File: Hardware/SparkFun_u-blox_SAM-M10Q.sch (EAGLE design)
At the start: 34 parts, among them J1 Qwiic Right Angle, J2 Qwiic Right Angle, J4 BOOT, U1 U-BLOX_SAM_M10Q-00B

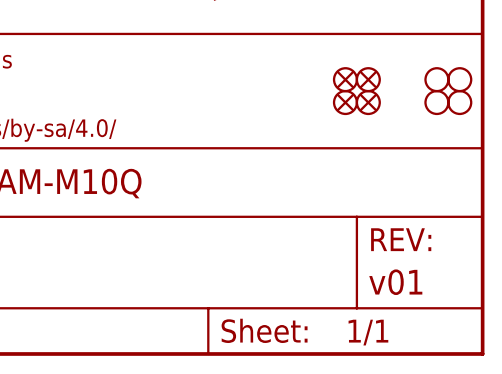
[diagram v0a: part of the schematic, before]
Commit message: Update for v10, Panelize. Add measures.
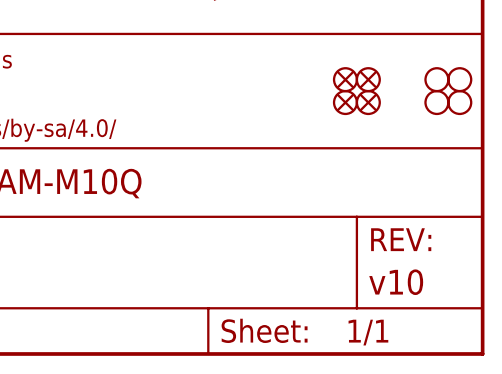
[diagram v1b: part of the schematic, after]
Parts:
- FRAME1: REV v01 -> v10
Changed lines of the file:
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@@
 <part name="FRAME1" library="SparkFun-Aesthetics" deviceset="FRAME-LETTER" device="">
 <attribute name="DESIGNER" value="Alex Brudner"/>
-<attribute name="REV" value="v01"/>
+<attribute name="REV" value="v10"/>
 </part>
 <part name="FD1" library="SparkFun-Aesthetics" deviceset="FIDUCIAL" device="UFIDUCIAL"/>

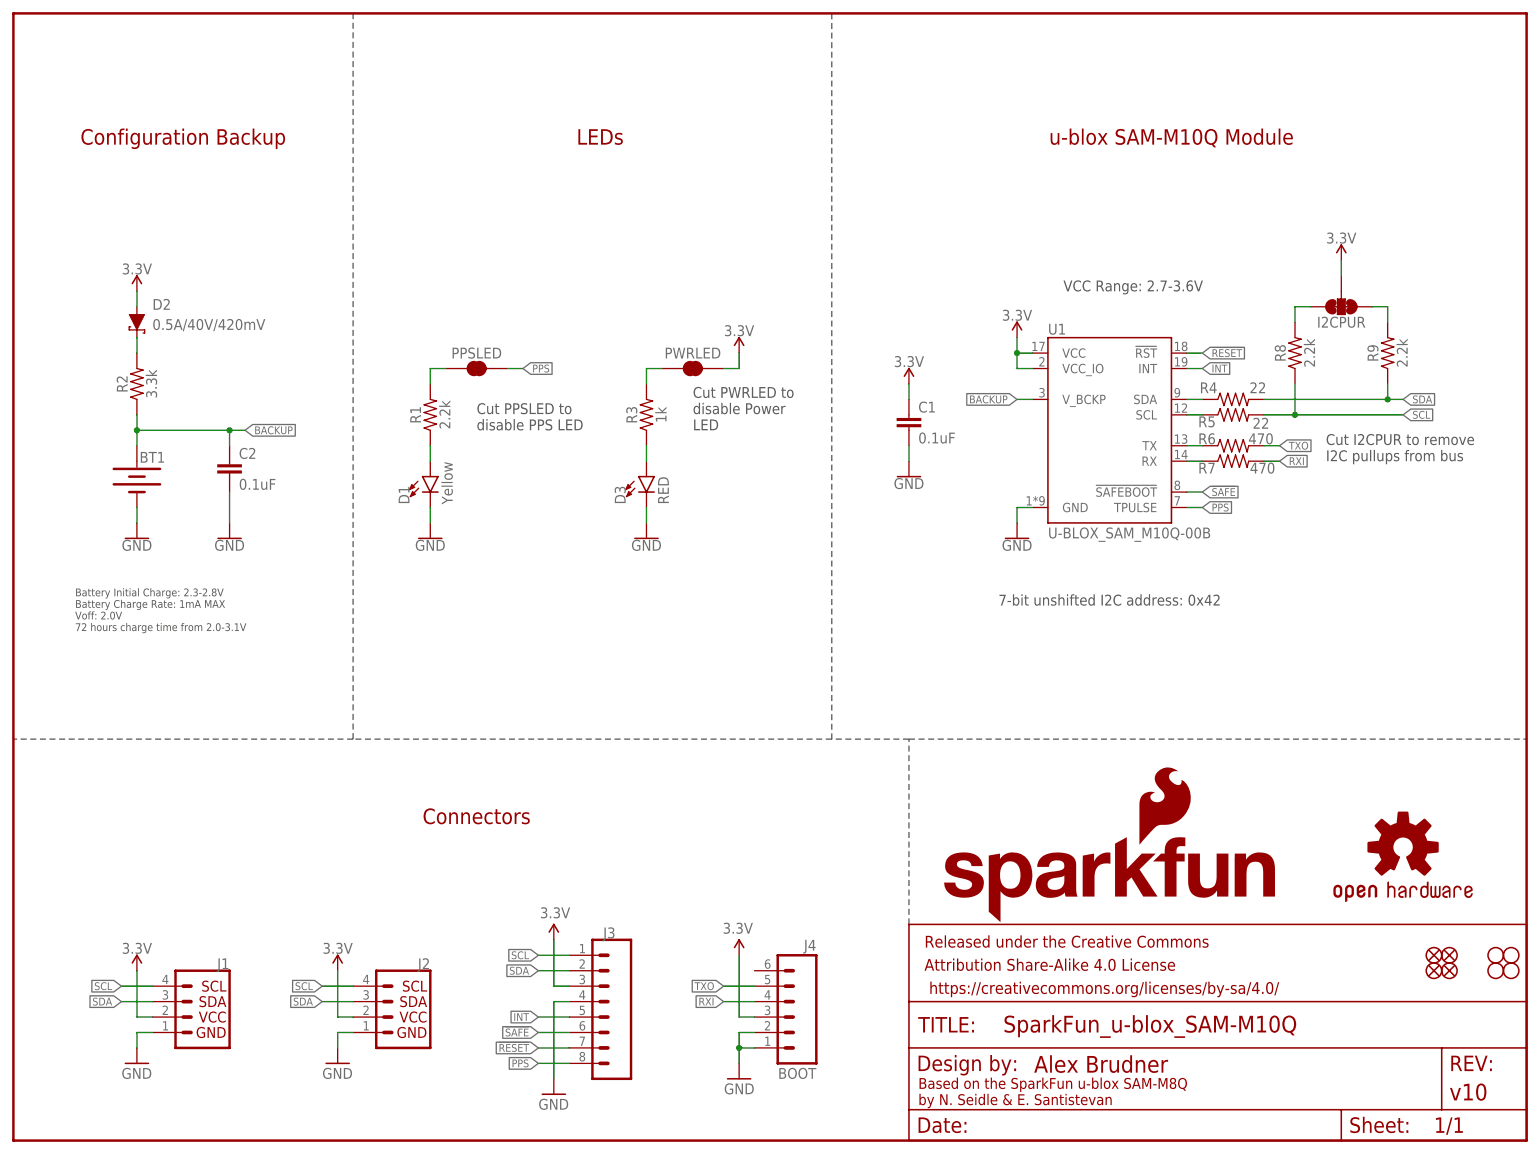
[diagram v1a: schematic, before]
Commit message: Update post design review.
Swap for updated reflowable battery.
Adjust note for battery accordingly.
Add qwiic symbol in schematic, replacing silk only on board.
Expand t/b keepout under M10Q.
Swap SCL/SDA silk so they are on the correct pins.
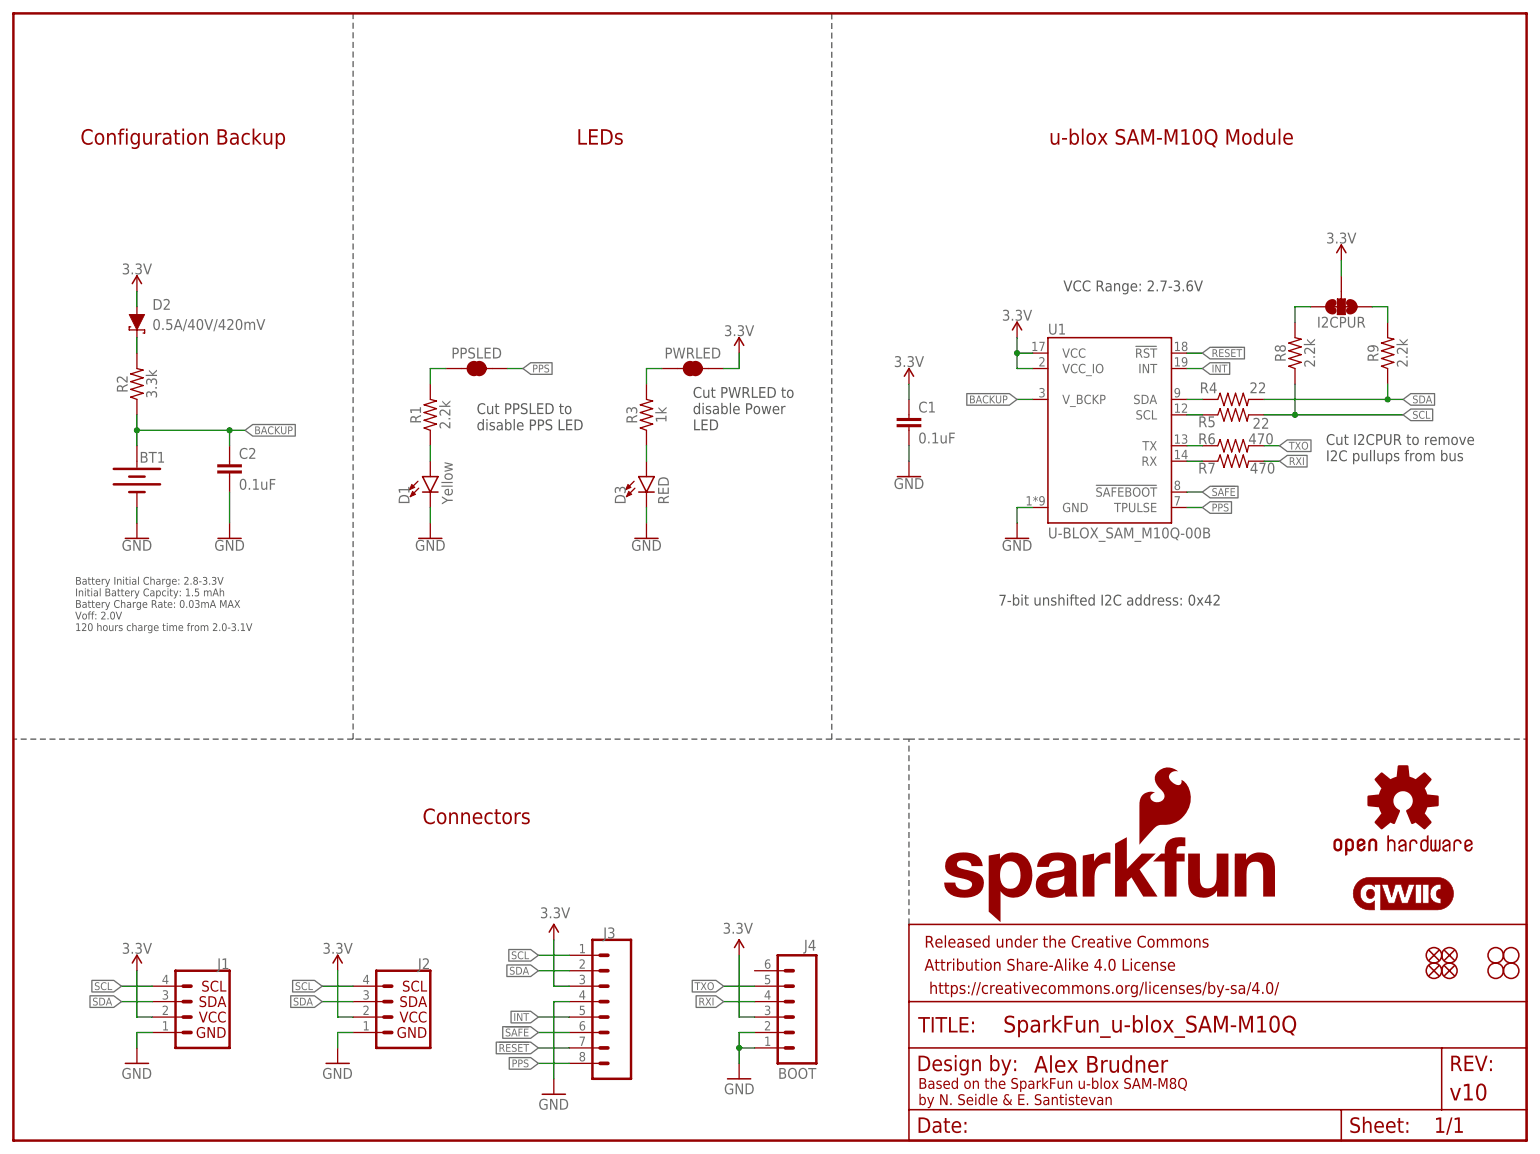
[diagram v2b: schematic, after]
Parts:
- added LOGO3: QWIIC_LOGO_CONNECTOR, SparkFun-Aesthetics:QWIIC_LOGO_CONNECTOR
- BT1: device SparkFun-Batteries:ML414H_IV01E_BATTERY -> SparkFun-Batteries:RELOWABLE_BATTERY_MS421R
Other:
- note added: "Battery Initial Charge: 2.8-3.3V Initial Battery Capcity: 1.5 mAh Battery Charge Rate: 0.03mA MAX Voff: 2.0V 120 hours charge time from 2.0-3.1V"
- note removed: "Battery Initial Charge: 2.3-2.8V Battery Charge Rate: 1mA MAX Voff: 2.0V 72 hours charge time from 2.0-3.1V"
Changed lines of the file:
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@@
 <part name="LOGO1" library="SparkFun-Aesthetics" deviceset="OSHW-LOGO" device="M"/>
 <part name="LOGO2" library="SparkFun-Aesthetics" deviceset="SFE_LOGO_NAME_FLAME" device=".2_INCH"/>
-<part name="BT1" library="SparkFun-Batteries" deviceset="ML414H_IV01E_BATTERY" device="" value="6.8MM_COIN_CELL"/>
+<part name="BT1" library="SparkFun-Batteries" deviceset="RELOWABLE_BATTERY" device="_MS421R" value="6.8MM_COIN_CELL"/>
 <part name="GND2" library="SparkFun-PowerSymbols" deviceset="GND" device=""/>
 <part name="GND4" library="SparkFun-PowerSymbols" deviceset="GND" device=""/>
@@
 <part name="C1" library="SparkFun-Capacitors" deviceset="0.1UF" device="-0603-25V-(+80/-20%)" value="0.1uF"/>
 <part name="C2" library="SparkFun-Capacitors" deviceset="0.1UF" device="-0603-25V-(+80/-20%)" value="0.1uF"/>
+<part name="LOGO3" library="SparkFun-Aesthetics" deviceset="QWIIC_LOGO" device="_CONNECTOR"/>
 </parts>
 <sheets>
@@
 <text x="148.844" y="5.842" size="1.778" layer="94" font="vector">Based on the SparkFun u-blox SAM-M8Q
 by N. Seidle &amp; E. Santistevan</text>
-<text x="10.16" y="83.82" size="1.27" layer="97" font="vector">Battery Initial Charge: 2.3-2.8V
-Battery Charge Rate: 1mA MAX
+<text x="10.16" y="83.82" size="1.27" layer="97" font="vector">Battery Initial Charge: 2.8-3.3V
+Initial Battery Capcity: 1.5 mAh
+Battery Charge Rate: 0.03mA MAX
 Voff: 2.0V
-72 hours charge time from 2.0-3.1V</text>
+120 hours charge time from 2.0-3.1V</text>
 <text x="180.34" y="88.9" size="1.778" layer="97" font="vector" align="center">7-bit unshifted I2C address: 0x42</text>
 <text x="215.9" y="111.76" size="1.778" layer="97" font="vector">Cut I2CPUR to remove
@@
 <instance part="H3" gate="G$1" x="243.84" y="27.94" smashed="yes"/>
 <instance part="H4" gate="G$1" x="243.84" y="30.48" smashed="yes"/>
-<instance part="LOGO1" gate="G$1" x="228.6" y="48.26" smashed="yes"/>
+<instance part="LOGO1" gate="G$1" x="228.6" y="55.88" smashed="yes"/>
 <instance part="LOGO2" gate="G$1" x="152.4" y="35.56" smashed="yes"/>
 <instance part="BT1" gate="G$1" x="20.32" y="109.22" smashed="yes" rot="R270">
@@
 <attribute name="VALUE" x="37.084" y="107.061" size="1.778" layer="96" font="vector"/>
 </instance>
+<instance part="LOGO3" gate="G$1" x="228.6" y="40.64" smashed="yes"/>
 </instances>
 <busses>

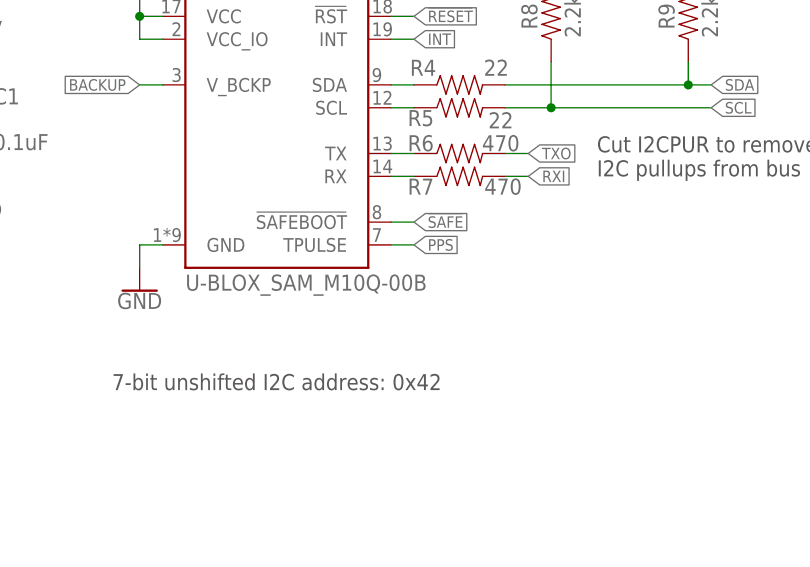
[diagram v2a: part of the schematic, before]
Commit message: Rework paste for DFM experiment.
Move original panel into 100_paste folder.
Repanelize with quad box paste and put into quad_paste folder.
Update library to have new variant.
Update sch and brd with new part.
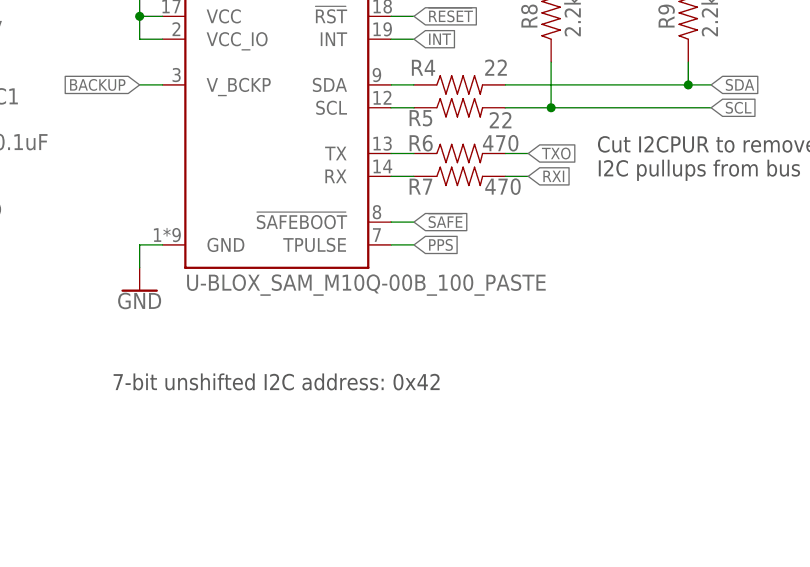
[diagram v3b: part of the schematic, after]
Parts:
- U1: value U-BLOX_SAM_M10Q-00B -> U-BLOX_SAM_M10Q-00B_100_PASTE; device u-blox_SAM-M10Q:U-BLOX_SAM_M10Q-00B -> u-blox_SAM-M10Q:U-BLOX_SAM_M10Q-00B_100_PASTE
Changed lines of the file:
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@@
 <part name="R5" library="SparkFun-Resistors" deviceset="22OHM" device="-0603-1/10W-1%" value="22"/>
 <part name="SUPPLY7" library="SparkFun-PowerSymbols" deviceset="3.3V" device=""/>
-<part name="U1" library="u-blox_SAM-M10Q" deviceset="U-BLOX_SAM_M10Q-00B" device=""/>
+<part name="U1" library="u-blox_SAM-M10Q" deviceset="U-BLOX_SAM_M10Q-00B" device="_100_PASTE" value="U-BLOX_SAM_M10Q-00B_100_PASTE"/>
 <part name="GND1" library="SparkFun-PowerSymbols" deviceset="GND" device=""/>
 <part name="D1" library="SparkFun-LED" deviceset="LED-YELLOW" device="0603" value="Yellow"/>

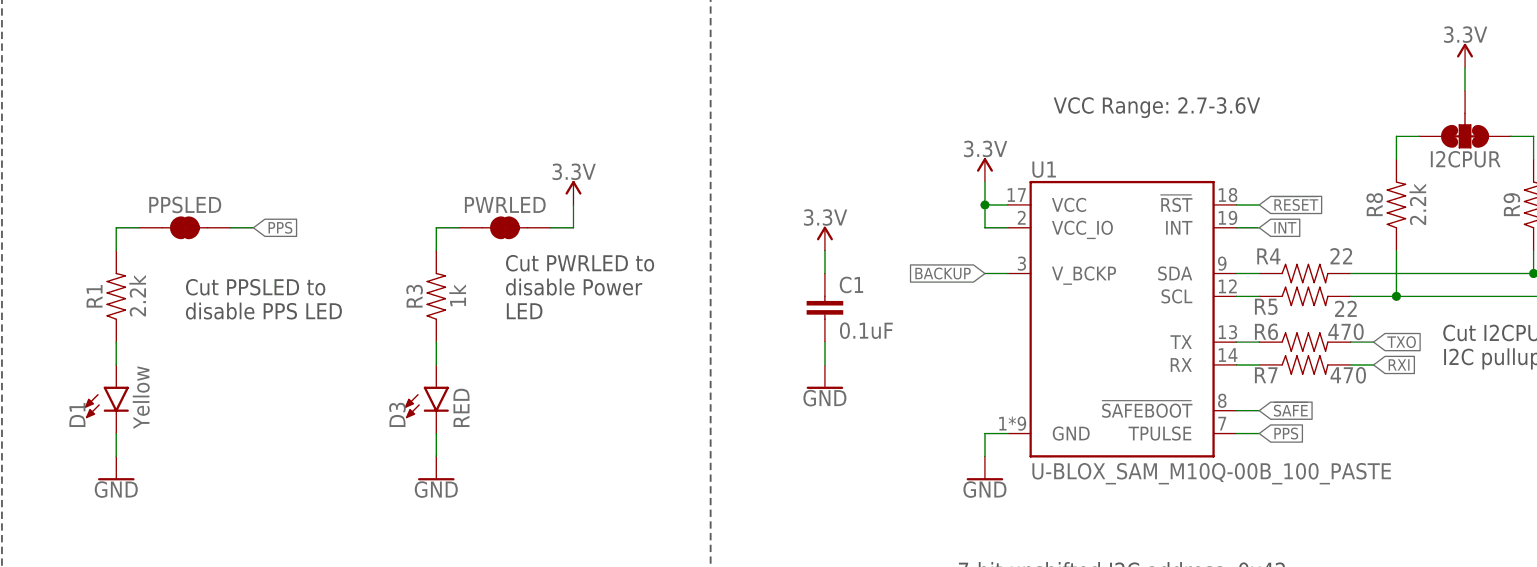
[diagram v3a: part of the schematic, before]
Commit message: Update for release
Remove quad paste part from lib.
Remove quad paste production folder.
Move 100 paste up one folder.
Update schematic/board for new part.
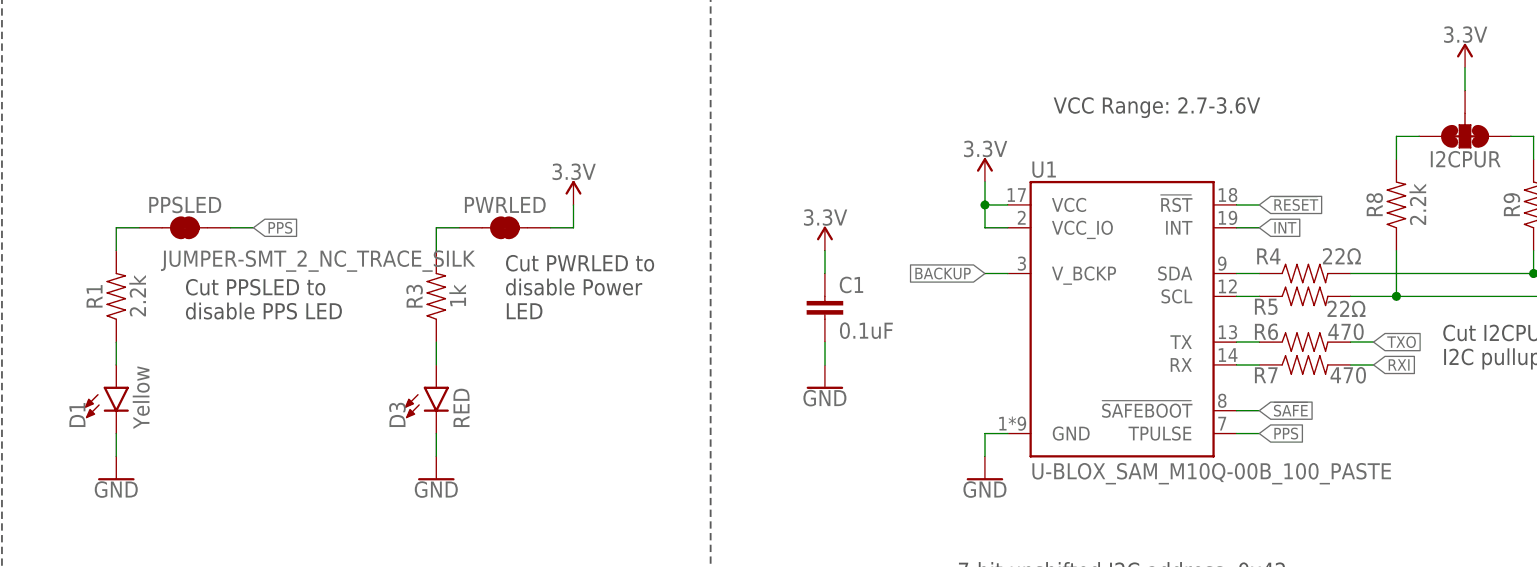
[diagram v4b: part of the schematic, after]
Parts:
- R4, R5: value 22 -> 22Ω
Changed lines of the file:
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@@
 <part name="R8" library="SparkFun-Resistors" deviceset="2.2KOHM" device="-0603-1/10W-1%" value="2.2k"/>
 <part name="R9" library="SparkFun-Resistors" deviceset="2.2KOHM" device="-0603-1/10W-1%" value="2.2k"/>
-<part name="I2CPUR" library="SparkFun-Jumpers" deviceset="JUMPER-SMT_3_2-NC_TRACE" device="_SILK" value="JUMPER-SMT_3_2-NC_TRACE_SILK"/>
+<part name="I2CPUR" library="SparkFun-Jumpers" deviceset="JUMPER-SMT_3_2-NC_TRACE" device="_SILK" package3d_urn="urn:adsk.eagle:package:39289/1" value="JUMPER-SMT_3_2-NC_TRACE_SILK"/>
 <part name="SUPPLY9" library="SparkFun-PowerSymbols" deviceset="3.3V" device=""/>
-<part name="R4" library="SparkFun-Resistors" deviceset="22OHM" device="-0603-1/10W-1%" value="22"/>
-<part name="R5" library="SparkFun-Resistors" deviceset="22OHM" device="-0603-1/10W-1%" value="22"/>
+<part name="R4" library="SparkFun-Resistors" deviceset="22OHM" device="-0603-1/10W-1%" value="22Ω"/>
+<part name="R5" library="SparkFun-Resistors" deviceset="22OHM" device="-0603-1/10W-1%" value="22Ω"/>
 <part name="SUPPLY7" library="SparkFun-PowerSymbols" deviceset="3.3V" device=""/>
 <part name="U1" library="u-blox_SAM-M10Q" deviceset="U-BLOX_SAM_M10Q-00B" device="_100_PASTE" value="U-BLOX_SAM_M10Q-00B_100_PASTE"/>
 <part name="GND1" library="SparkFun-PowerSymbols" deviceset="GND" device=""/>
 <part name="D1" library="SparkFun-LED" deviceset="LED-YELLOW" device="0603" value="Yellow"/>
-<part name="PPSLED" library="SparkFun-Jumpers" deviceset="JUMPER-SMT_2_NC_TRACE" device="_SILK" value=""/>
+<part name="PPSLED" library="SparkFun-Jumpers" deviceset="JUMPER-SMT_2_NC_TRACE" device="_SILK" package3d_urn="urn:adsk.eagle:package:39281/1" value="JUMPER-SMT_2_NC_TRACE_SILK"/>
 <part name="R3" library="SparkFun-Resistors" deviceset="1KOHM" device="-0603-1/10W-1%" value="1k"/>
 <part name="D3" library="SparkFun-LED" deviceset="LED-RED" device="0603" value="RED"/>
-<part name="PWRLED" library="SparkFun-Jumpers" deviceset="JUMPER-SMT_2_NC_TRACE" device="_SILK"/>
+<part name="PWRLED" library="SparkFun-Jumpers" deviceset="JUMPER-SMT_2_NC_TRACE" device="_SILK" package3d_urn="urn:adsk.eagle:package:39281/1"/>
 <part name="GND3" library="SparkFun-PowerSymbols" deviceset="GND" device=""/>
 <part name="SUPPLY2" library="SparkFun-PowerSymbols" deviceset="3.3V" device=""/>
@@
 <attribute name="VALUE" x="121.92" y="7.62" size="1.778" layer="96" font="vector" rot="MR0"/>
 </instance>
-<instance part="J4" gate="G$1" x="127" y="20.32" smashed="yes" rot="MR0">
+<instance part="J4" gate="JP1" x="127" y="20.32" smashed="yes" rot="MR0">
 <attribute name="VALUE" x="132.08" y="10.16" size="1.778" layer="96" font="vector" rot="MR0"/>
 <attribute name="NAME" x="132.08" y="31.242" size="1.778" layer="95" font="vector" rot="MR0"/>
@@
 </segment>
 <segment>
-<pinref part="J4" gate="G$1" pin="3"/>
+<pinref part="J4" gate="JP1" pin="3"/>
 <wire x1="121.92" y1="20.32" x2="119.38" y2="20.32" width="0.1524" layer="91"/>
 <wire x1="119.38" y1="20.32" x2="119.38" y2="30.48" width="0.1524" layer="91"/>
@@
 <wire x1="121.92" y1="15.24" x2="119.38" y2="15.24" width="0.1524" layer="91"/>
 <junction x="119.38" y="15.24"/>
-<pinref part="J4" gate="G$1" pin="1"/>
-<pinref part="J4" gate="G$1" pin="2"/>
+<pinref part="J4" gate="JP1" pin="1"/>
+<pinref part="J4" gate="JP1" pin="2"/>
 </segment>
 <segment>
@@
 <wire x1="121.92" y1="22.86" x2="116.84" y2="22.86" width="0.1524" layer="91"/>
 <label x="116.84" y="22.86" size="1.27" layer="95" font="vector" rot="R180" xref="yes"/>
-<pinref part="J4" gate="G$1" pin="4"/>
+<pinref part="J4" gate="JP1" pin="4"/>
 </segment>
 </net>
@@
 <wire x1="121.92" y1="25.4" x2="116.84" y2="25.4" width="0.1524" layer="91"/>
 <label x="116.84" y="25.4" size="1.27" layer="95" font="vector" rot="R180" xref="yes"/>
-<pinref part="J4" gate="G$1" pin="5"/>
+<pinref part="J4" gate="JP1" pin="5"/>
 </segment>
 </net>
@@
 which will not be processed correctly with this version.
 </note>
+<note version="8.3" severity="warning">
+Since Version 8.3, EAGLE supports URNs for individual library
+assets (packages, symbols, and devices). The URNs of those assets
+will not be understood (or retained) with this version.
+</note>
+<note version="8.3" severity="warning">
+Since Version 8.3, EAGLE supports the association of 3D packages
+with devices in libraries, schematics, and board files. Those 3D
+packages will not be understood (or retained) with this version.
+</note>
 </compatibility>
